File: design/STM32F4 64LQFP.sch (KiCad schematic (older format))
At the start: 15 parts, among them P2 SWD, U1 STM32F40X_LQFP64, X2 8MHz 10ppm

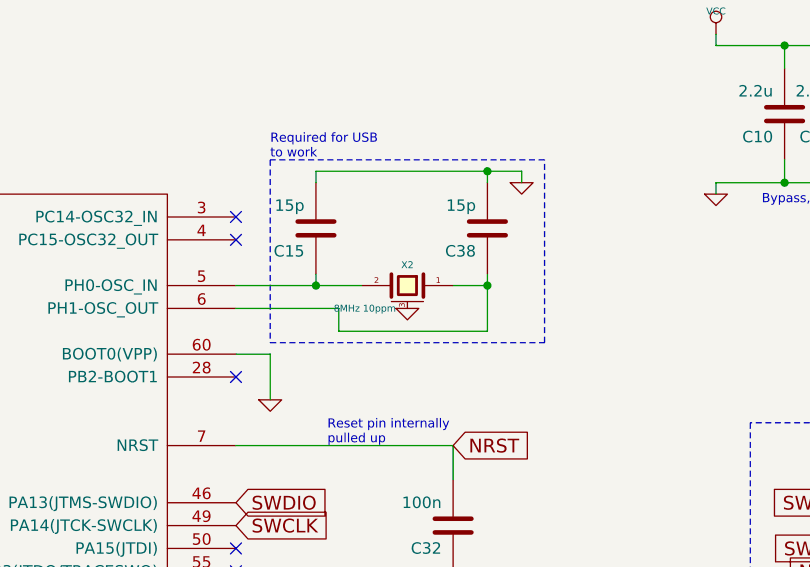
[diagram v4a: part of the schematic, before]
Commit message: Fixed Crystal connection and footprint
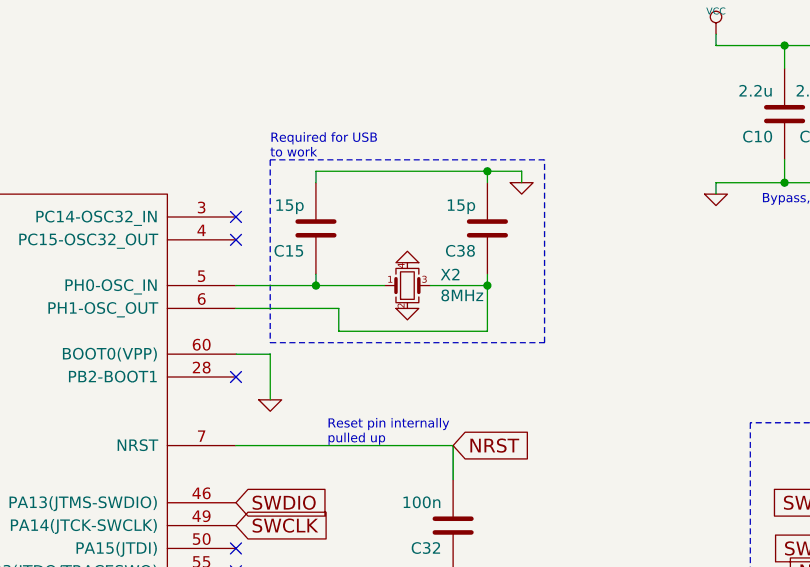
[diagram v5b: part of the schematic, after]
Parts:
- removed X2: 8MHz 10ppm, Crystal:Crystal_SMD_5032-4Pin_5.0x3.2mm, symbol BLDC_4-rescue:CRYSTAL_SMD
- added X2: 8MHz, Crystal:Crystal_SMD_Abracon_ABM3B-4Pin_5.0x3.2mm, symbol Device:Crystal_GND24_Small
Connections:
- net GND: now also X2.2, X2.4
- net at C15.1, U1.5 (PH0-OSC_IN): now also X2.1
- net at C38.1, U1.6 (PH1-OSC_OUT): now also X2.3
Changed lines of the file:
@@
 Connection ~ 8100 2050
 Wire Wire Line
-	7950 2050 8100 2050
-Wire Wire Line
 	8100 2000 8100 2050
 Wire Wire Line
@@
 LED_GREEN
 $Comp
-L BLDC_4-rescue:CRYSTAL_SMD X2
-U 1 1 540978A3
-P 7750 2050
-F 0 "X2" H 7750 2140 30  0000 C CNN
-F 1 "8MHz 10ppm" H 7800 1950 30  0000 L CNN
-F 2 "Crystal:Crystal_SMD_5032-4Pin_5.0x3.2mm" H 7750 2050 60  0001 C CNN
-F 3 "" H 7750 2050 60  0000 C CNN
-F 4 "ABM3B-8.0-10-1UT" H 7750 2050 60  0001 C CNN "mfg#"
-	1    7750 2050
-	-1   0    0    -1
-$EndComp
-$Comp
 L BLDC_4-rescue:GND-RESCUE-BLDC_4 #PWR043
 U 1 1 54097D19
@@
 	8100 1550 8250 1550
 Wire Wire Line
-	7350 2050 7550 2050
-Wire Wire Line
 	8100 2050 8100 2250
 Wire Wire Line
@@
 NoConn ~ 4500 5650
 NoConn ~ 4500 2050
+$Comp
+L Device:Crystal_GND24_Small X2
+U 1 1 5E46CEBB
+P 7750 2050
+F 0 "X2" H 7894 2096 50  0000 L CNN
+F 1 "8MHz" H 7894 2005 50  0000 L CNN
+F 2 "Crystal:Crystal_SMD_Abracon_ABM3B-4Pin_5.0x3.2mm" H 7750 2050 50  0001 C CNN
+F 3 "~" H 7750 2050 50  0001 C CNN
+	1    7750 2050
+	1    0    0    -1
+$EndComp
+Wire Wire Line
+	7350 2050 7650 2050
+Wire Wire Line
+	7850 2050 8100 2050
+$Comp
+L BLDC_4-rescue:GND-RESCUE-BLDC_4 #PWR?
+U 1 1 5E470F26
+P 7750 1950
+F 0 "#PWR?" H 7750 1950 30  0001 C CNN
+F 1 "GND" H 7750 1880 30  0001 C CNN
+F 2 "" H 7750 1950 60  0001 C CNN
+F 3 "" H 7750 1950 60  0001 C CNN
+	1    7750 1950
+	-1   0    0    1
+$EndComp
 $EndSCHEMATC
